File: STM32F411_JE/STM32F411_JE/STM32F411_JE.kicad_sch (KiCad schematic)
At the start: 32 parts, among them J1 USB4105-GF-A, J2 Screw_Terminal_01x04, J3 Conn_01x20_Socket, J4 Conn_01x20_Socket, SW1 SW_Push, SW2 SW_Push, U1 STM32F411CEU6, U2 AP7343, Y1 25 Mhz

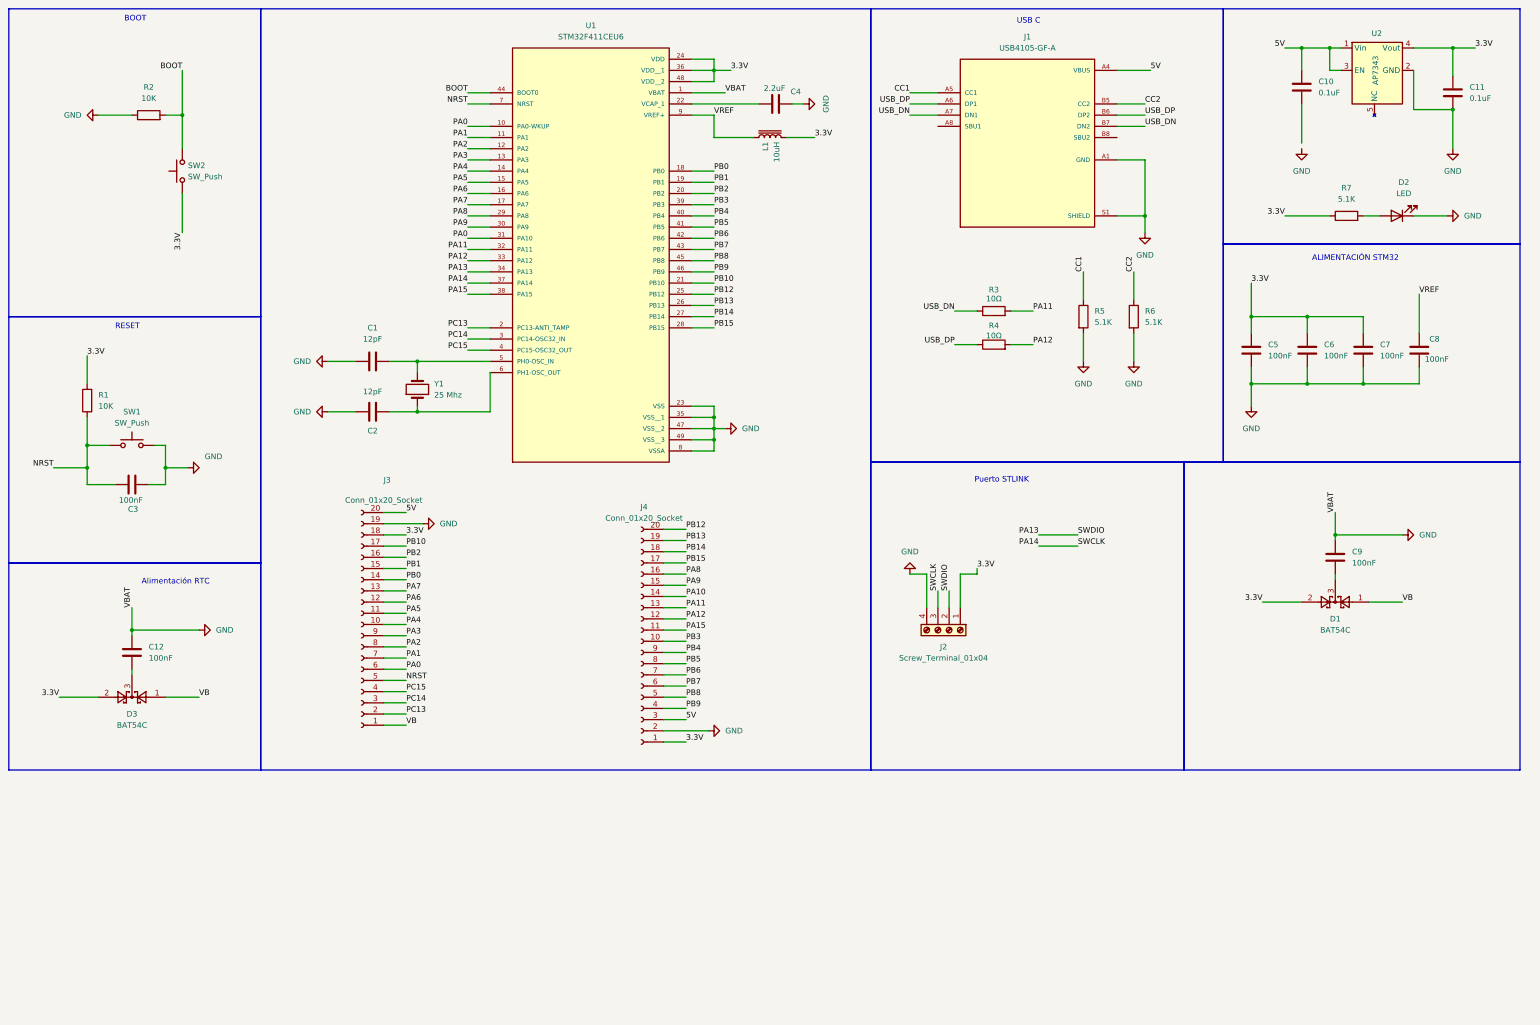
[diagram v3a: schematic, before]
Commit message: Se termina el diseño de la zona de cobre de la pcb
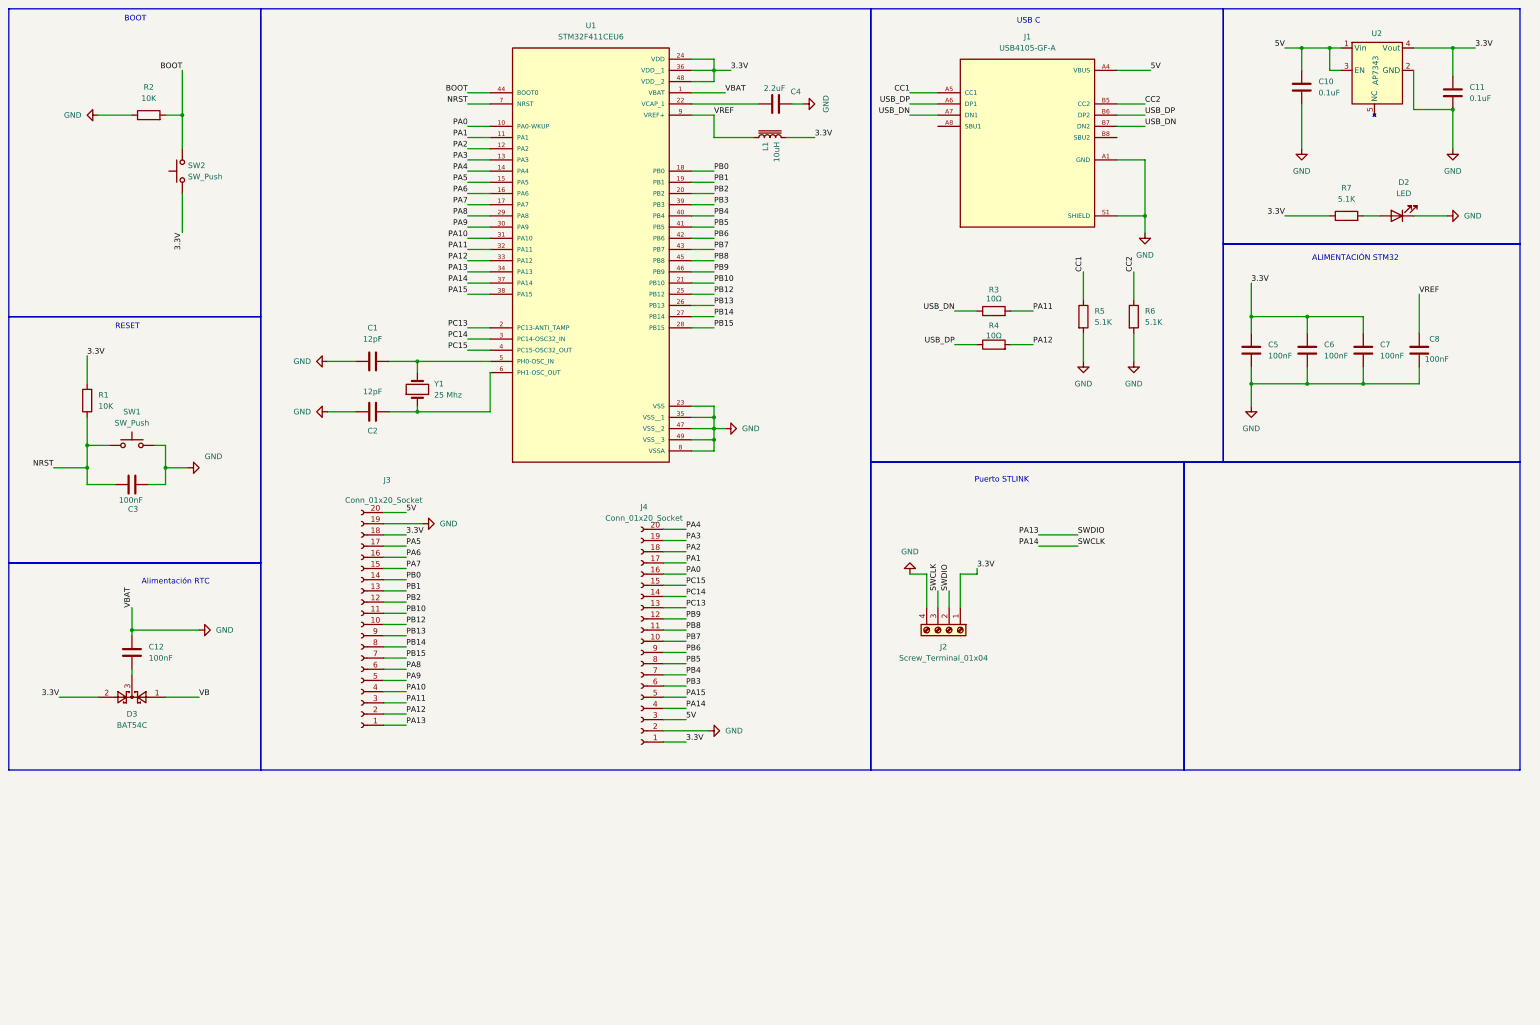
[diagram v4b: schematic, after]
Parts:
- removed C9: 100nF, Capacitor_SMD:C_0603_1608Metric_Pad1.08x0.95mm_HandSolder, symbol Device:C
- removed D1: BAT54C, Package_TO_SOT_SMD:SOT-23, symbol Diode:BAT54C
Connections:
- net GND: now also C10.2
- net NRST: no longer J3.5 (Pin_5)
- net PA0: now also J4.16 (Pin_16); no longer J3.6 (Pin_6), U1.31 (PA10)
- net PA1: now also J4.17 (Pin_17); no longer J3.7 (Pin_7)
- net PA10: now also J3.4 (Pin_4), U1.31 (PA10); no longer J4.14 (Pin_14)
- net PA11: now also J3.3 (Pin_3); no longer J4.13 (Pin_13)
- net PA12: now also J3.2 (Pin_2); no longer J4.12 (Pin_12)
- net PA13: now also J3.1 (Pin_1)
- net PA14: now also J4.4 (Pin_4)
- net PA15: now also J4.5 (Pin_5); no longer J4.11 (Pin_11)
- net PA2: now also J4.18 (Pin_18); no longer J3.8 (Pin_8)
- net PA3: now also J4.19 (Pin_19); no longer J3.9 (Pin_9)
- net PA4: now also J4.20 (Pin_20); no longer J3.10 (Pin_10)
- net PA5: now also J3.17 (Pin_17); no longer J3.11 (Pin_11)
- net PA6: now also J3.16 (Pin_16); no longer J3.12 (Pin_12)
- net PA7: now also J3.15 (Pin_15); no longer J3.13 (Pin_13)
- net PA8: now also J3.6 (Pin_6); no longer J4.16 (Pin_16)
- net PA9: now also J3.5 (Pin_5); no longer J4.15 (Pin_15)
- net PB1: now also J3.13 (Pin_13); no longer J3.15 (Pin_15)
- net PB10: now also J3.11 (Pin_11); no longer J3.17 (Pin_17)
- net PB12: now also J3.10 (Pin_10); no longer J4.20 (Pin_20)
- net PB13: now also J3.9 (Pin_9); no longer J4.19 (Pin_19)
- net PB14: now also J3.8 (Pin_8); no longer J4.18 (Pin_18)
- net PB15: now also J3.7 (Pin_7); no longer J4.17 (Pin_17)
- net PB2: now also J3.12 (Pin_12); no longer J3.16 (Pin_16)
- net PB3: now also J4.6 (Pin_6); no longer J4.10 (Pin_10)
- net PB4: now also J4.7 (Pin_7); no longer J4.9 (Pin_9)
- net PB6: now also J4.9 (Pin_9); no longer J4.7 (Pin_7)
- net PB7: now also J4.10 (Pin_10); no longer J4.6 (Pin_6)
- net PB8: now also J4.11 (Pin_11); no longer J4.5 (Pin_5)
- net PB9: now also J4.12 (Pin_12); no longer J4.4 (Pin_4)
- net PC13: now also J4.13 (Pin_13); no longer J3.2 (Pin_2)
- net PC14: now also J4.14 (Pin_14); no longer J3.3 (Pin_3)
- net PC15: now also J4.15 (Pin_15); no longer J3.4 (Pin_4)
- net VB: no longer J3.1 (Pin_1)
